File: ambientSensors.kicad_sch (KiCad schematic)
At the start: 13 parts, among them J2 BM04B-SRSS-TB, U1 LTR-329ALS-01, U3 TPS22914BYFPR, U7 BME688

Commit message: rev2 precheck DRC clean
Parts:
- TP10, TP9: footprint TestPoint:TestPoint_Pad_D1.0mm -> TestPoint:TestPoint_THTPad_1.0x1.0mm_Drill0.5mm
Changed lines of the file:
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@@
 			)
 		)
-		(property "Footprint" "TestPoint:TestPoint_Pad_D1.0mm"
+		(property "Footprint" "TestPoint:TestPoint_THTPad_1.0x1.0mm_Drill0.5mm"
 			(at 223.52 97.79 0)
 			(effects
@@
 			)
 		)
-		(property "Footprint" "TestPoint:TestPoint_Pad_D1.0mm"
+		(property "Footprint" "TestPoint:TestPoint_THTPad_1.0x1.0mm_Drill0.5mm"
 			(at 219.71 95.25 0)
 			(effects

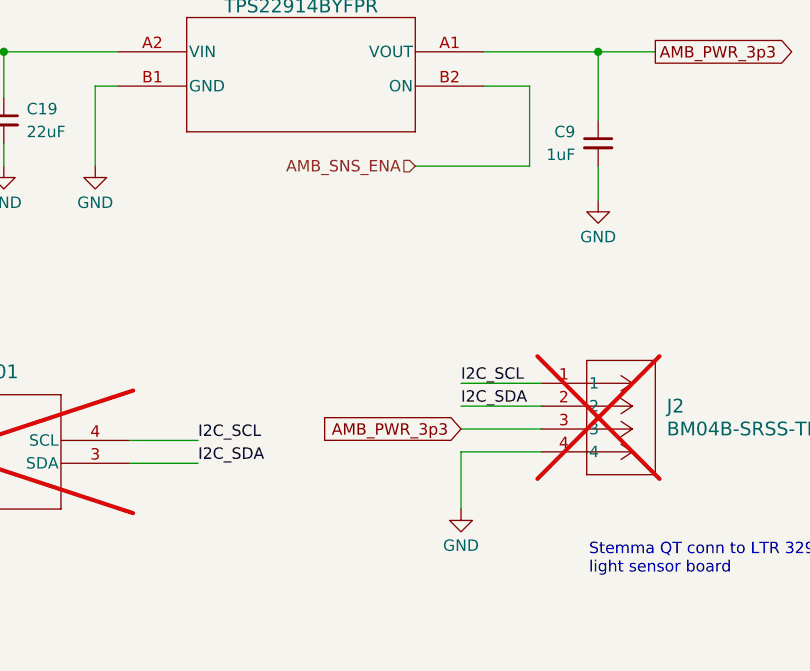
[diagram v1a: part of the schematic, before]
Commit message: updated schematic for pwr savings
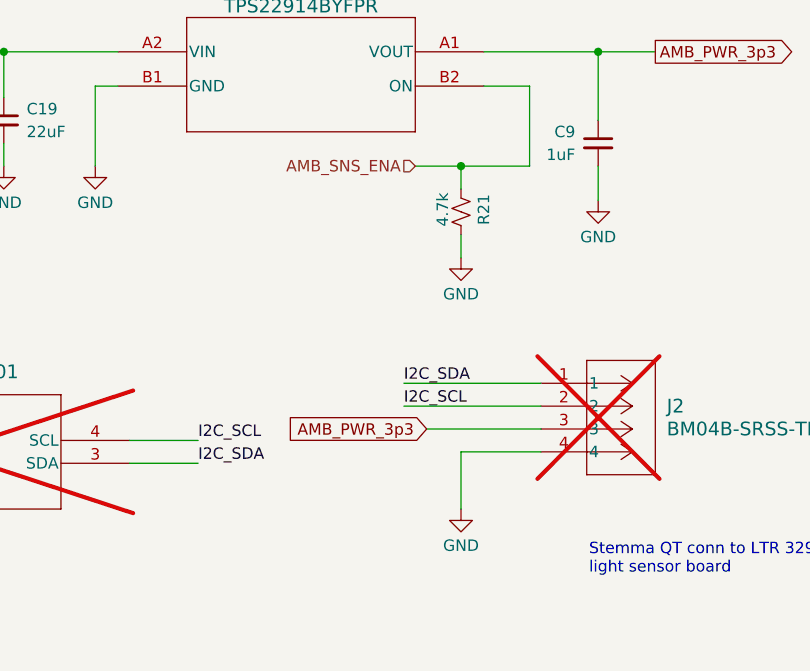
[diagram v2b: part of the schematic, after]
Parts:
- added R21: 4.7k, Resistor_SMD:R_0402_1005Metric, symbol Device:R_Small_US
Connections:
- net AMB_SNS_ENA: now also R21.2
- net GND: now also R21.1
- net I2C_SCL: now also J2.2; no longer J2.1
- net I2C_SDA: now also J2.1; no longer J2.2
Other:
- title: SproutSyncProto-A-01 -> SproutSyncProto-A-02

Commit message: updated pcb for pwr savings
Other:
- title: SproutSyncProto-A-02 -> SproutSyncProto-A-04
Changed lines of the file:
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@@
 	(paper "A4")
 	(title_block
-		(title "SproutSyncProto-A-02")
-		(date "2026-04-29")
+		(title "SproutSyncProto-A-04")
+		(date "2026-05-04")
 		(rev "0.2")
 		(company "SproutSync LTD")
